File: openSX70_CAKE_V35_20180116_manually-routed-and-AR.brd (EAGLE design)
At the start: 95.9 x 27.9 mm, 38 parts, among them Q1 5.8A/30V/35mΩ, Q2 5.8A/30V/35mΩ, U1 ATMEGA328P_TQFP, U3 BH1750FVI-TR, Y1 CSTCE16M0V53-R0

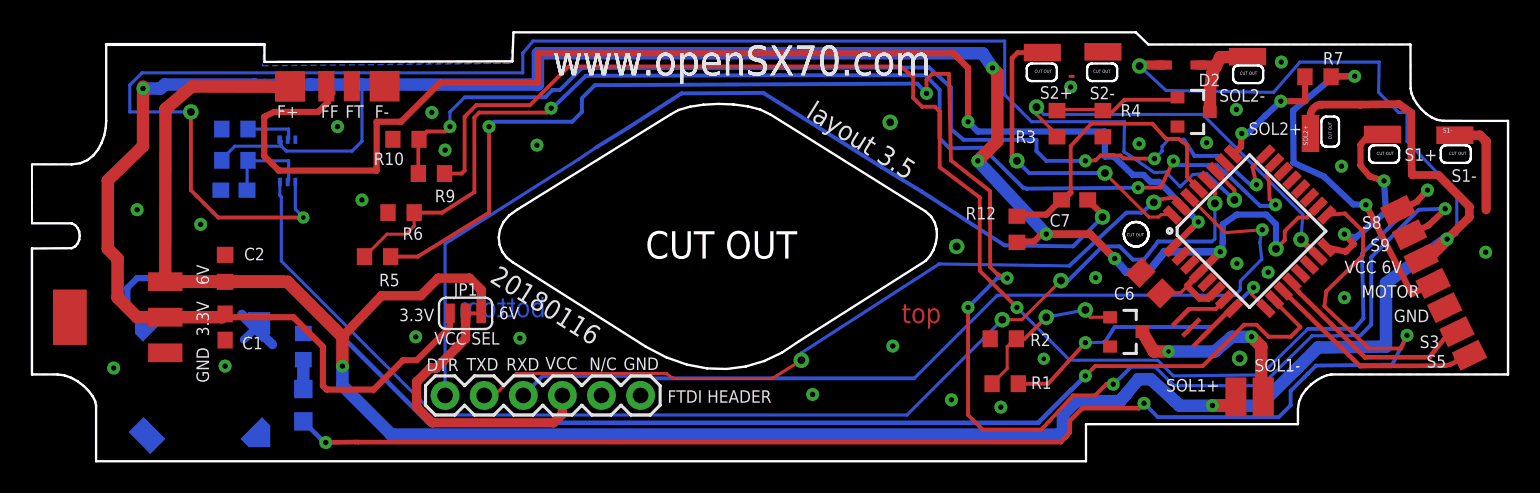
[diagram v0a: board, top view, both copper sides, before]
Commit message: Lots of small fixes, and fixed cosmetically values, widening track and such.
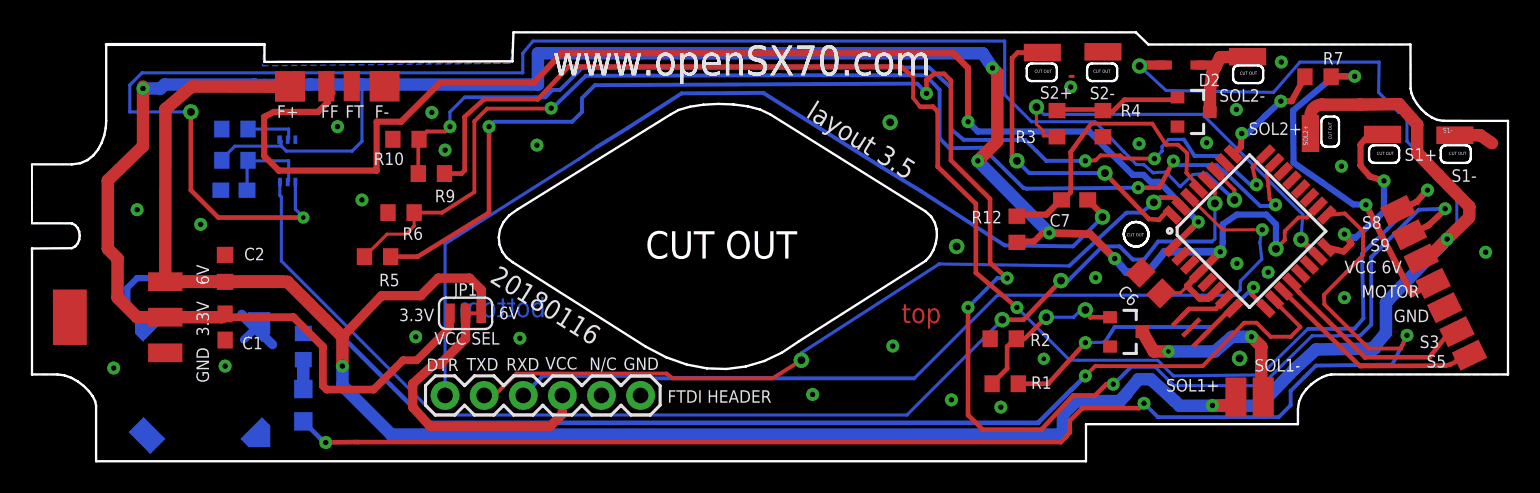
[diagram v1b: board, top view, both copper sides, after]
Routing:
- net GND: track 12.3 -> 8.20 mm
- net FF: track 85.7 -> 83.7 mm
- net 6V: track 187.9 -> 186.1 mm
- net SDA: track 105.5 -> 104.5 mm
- net MOTOR+: track 8.11 -> 7.45 mm
- net N$27: track 19.0 -> 19.6 mm
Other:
- board text added: "A+"
